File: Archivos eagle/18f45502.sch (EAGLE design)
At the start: 27 parts, among them IC1 PIC18F4550_40, IC2 7805DT, Q1 20MHz, X1 DCJ0202, X2 PN61729-S

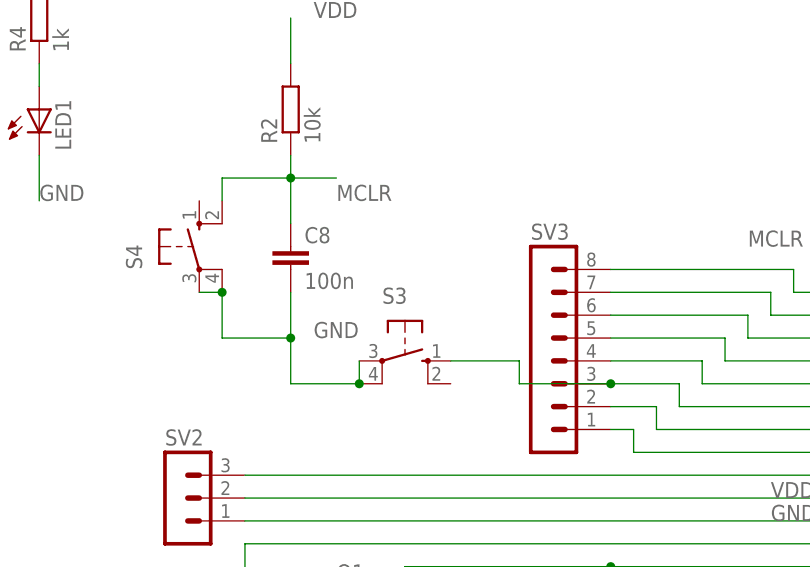
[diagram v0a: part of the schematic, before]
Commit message: build alpha 1.3
se acomodaron los agujeros porque estaban tocando el borde de la placa y
los pulsadores se re ubicaron de una forma simetrica
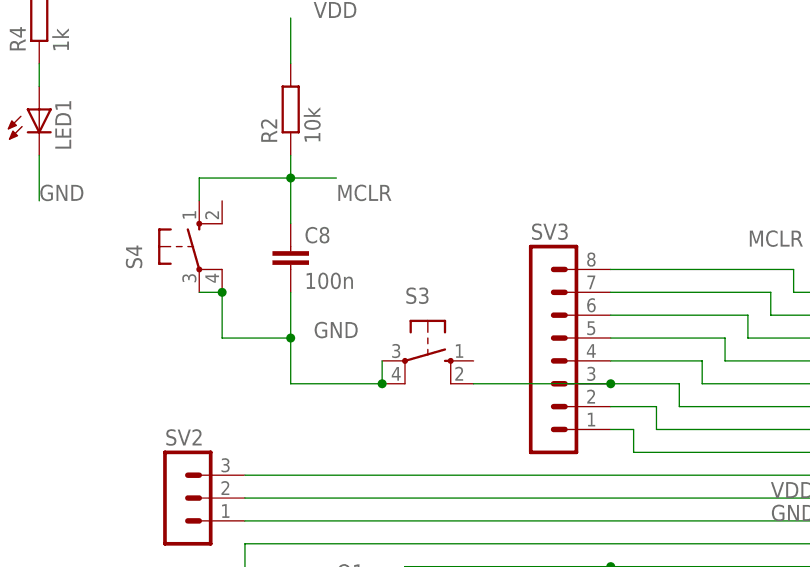
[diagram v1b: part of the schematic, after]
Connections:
- net MCLR: now also S4.S; no longer S4.S1
- net N$18: now also S3.S1; no longer S3.S
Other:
- moved on the sheet: S3
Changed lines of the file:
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@@
 <instance part="LED1" gate="G$1" x="-58.42" y="101.6"/>
 <instance part="R4" gate="G$1" x="-58.42" y="111.76" rot="R90"/>
-<instance part="S3" gate="1" x="-17.78" y="73.66" rot="R270"/>
+<instance part="S3" gate="1" x="-15.24" y="73.66" rot="R270"/>
 <instance part="S4" gate="1" x="-40.64" y="86.36"/>
 <instance part="IC2" gate="A1" x="114.3" y="132.08"/>
@@
 <wire x1="-30.48" y1="96.52" x2="-30.48" y2="93.98" width="0.1524" layer="91"/>
 <wire x1="-30.48" y1="93.98" x2="-30.48" y2="88.9" width="0.1524" layer="91"/>
-<wire x1="-38.1" y1="91.44" x2="-38.1" y2="93.98" width="0.1524" layer="91"/>
-<wire x1="-38.1" y1="93.98" x2="-30.48" y2="93.98" width="0.1524" layer="91"/>
+<wire x1="-40.64" y1="93.98" x2="-30.48" y2="93.98" width="0.1524" layer="91"/>
 <junction x="-30.48" y="93.98"/>
 <label x="-25.4" y="91.44" size="1.778" layer="95"/>
 <pinref part="R2" gate="G$1" pin="1"/>
 <pinref part="C8" gate="G$1" pin="1"/>
-<pinref part="S4" gate="1" pin="S1"/>
+<pinref part="S4" gate="1" pin="S"/>
+<wire x1="-40.64" y1="91.44" x2="-40.64" y2="93.98" width="0.1524" layer="91"/>
 </segment>
 <segment>
@@
 <segment>
 <wire x1="-30.48" y1="76.2" x2="-30.48" y2="81.28" width="0.1524" layer="91"/>
-<wire x1="-22.86" y1="71.12" x2="-30.48" y2="71.12" width="0.1524" layer="91"/>
+<wire x1="-20.32" y1="71.12" x2="-30.48" y2="71.12" width="0.1524" layer="91"/>
 <wire x1="-30.48" y1="71.12" x2="-30.48" y2="76.2" width="0.1524" layer="91"/>
 <wire x1="-38.1" y1="76.2" x2="-30.48" y2="76.2" width="0.1524" layer="91"/>
 <wire x1="-38.1" y1="76.2" x2="-38.1" y2="81.28" width="0.1524" layer="91"/>
 <wire x1="-40.64" y1="81.28" x2="-38.1" y2="81.28" width="0.1524" layer="91"/>
-<wire x1="-22.86" y1="73.66" x2="-22.86" y2="71.12" width="0.1524" layer="91"/>
+<wire x1="-20.32" y1="73.66" x2="-20.32" y2="71.12" width="0.1524" layer="91"/>
 <junction x="-30.48" y="76.2"/>
 <junction x="-38.1" y="81.28"/>
-<junction x="-22.86" y="71.12"/>
+<junction x="-20.32" y="71.12"/>
 <label x="-27.94" y="76.2" size="1.778" layer="95"/>
 <pinref part="C8" gate="G$1" pin="2"/>
@@
 <wire x1="12.7" y1="68.58" x2="12.7" y2="71.12" width="0.1524" layer="91"/>
 <wire x1="12.7" y1="71.12" x2="5.08" y2="71.12" width="0.1524" layer="91"/>
-<wire x1="-5.08" y1="71.12" x2="5.08" y2="71.12" width="0.1524" layer="91"/>
-<wire x1="-12.7" y1="73.66" x2="-5.08" y2="73.66" width="0.1524" layer="91"/>
-<wire x1="-5.08" y1="73.66" x2="-5.08" y2="71.12" width="0.1524" layer="91"/>
+<wire x1="-10.16" y1="71.12" x2="5.08" y2="71.12" width="0.1524" layer="91"/>
 <junction x="5.08" y="71.12"/>
 <pinref part="IC1" gate="G$1" pin="RA5/AN4/!SS!/HLVDIN/C2OUT"/>
 <pinref part="SV3" gate="1" pin="3"/>
-<pinref part="S3" gate="1" pin="S"/>
-</segment>
-</net>
+<pinref part="S3" gate="1" pin="S1"/>
+</segment>
+</net>
